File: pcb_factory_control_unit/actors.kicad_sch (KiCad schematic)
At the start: 65 parts, among them J17 STEP1, J18 STEP2, J30 Valve, Q1 IRLML6344, Q2 IRLML6344, Q3 IRLML6344, Q5 IRLML6344, Q6 IRLML6344, U11 74AHCT125, U7 TMC2209, U8 TMC2209

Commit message: Changed LED ReverseMount Footprint, Removed PullUp, HSOS Logo
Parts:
- D2, D3, D4, D5, D8: footprint liebler_OPTO:LED_1206_3216Metric_ReverseMount -> LED_SMD:LED_1206_3216Metric_ReverseMount_Hole1.8x2.4mm

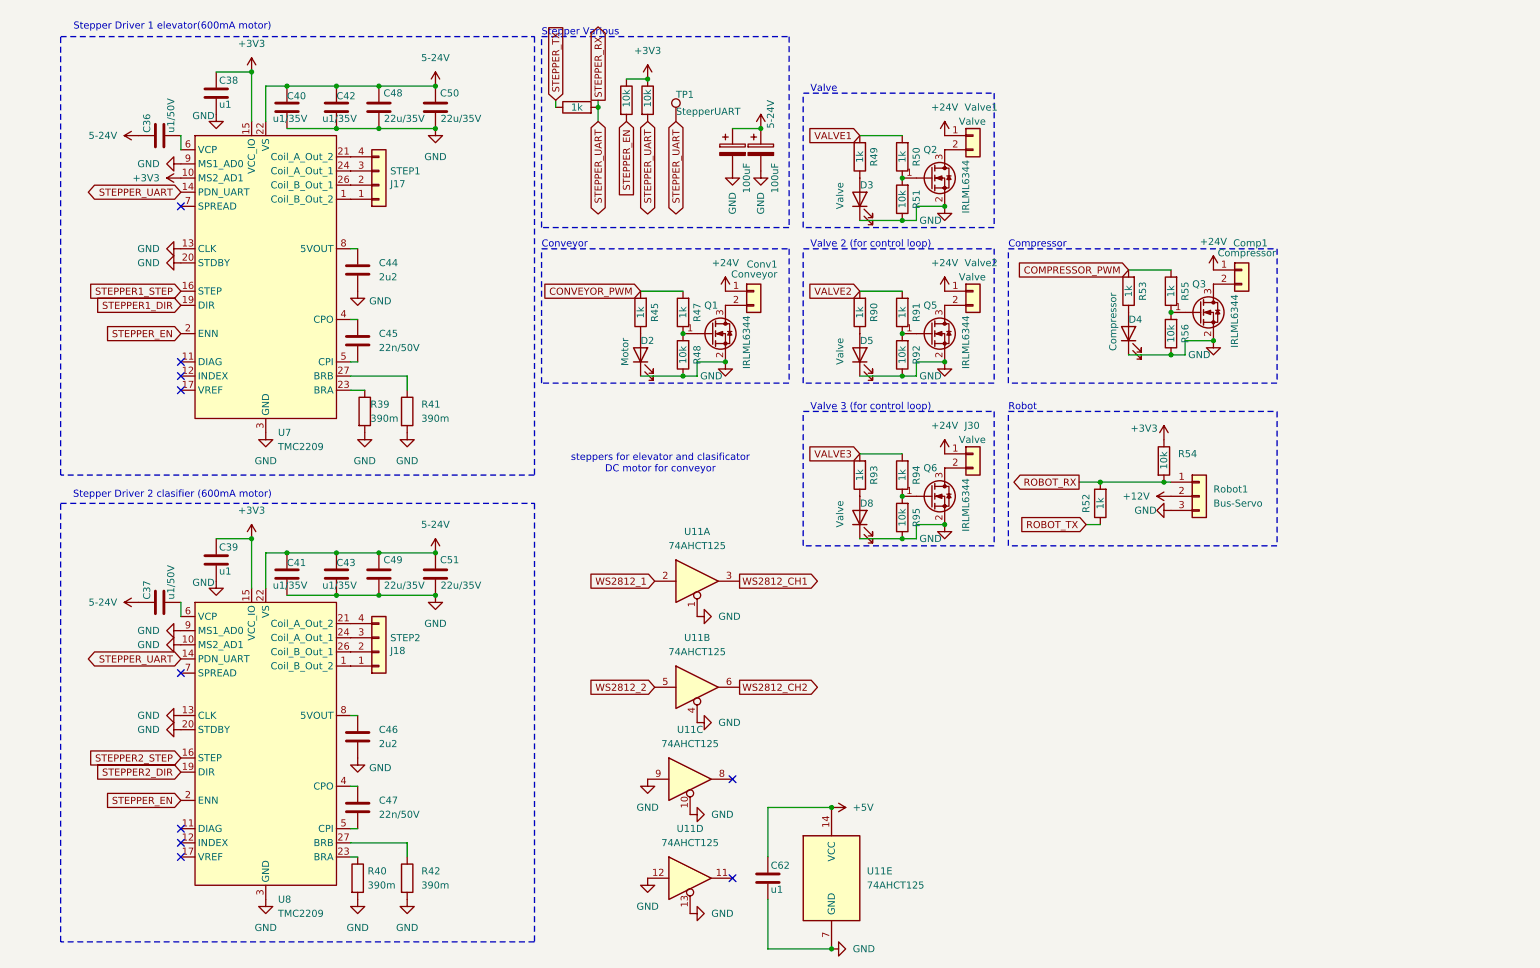
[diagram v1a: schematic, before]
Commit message: Control Unit PCB: schematic rework (PSU, MX26631DL, XL6009 module, ERC fixes), new placement on 90 mm high board
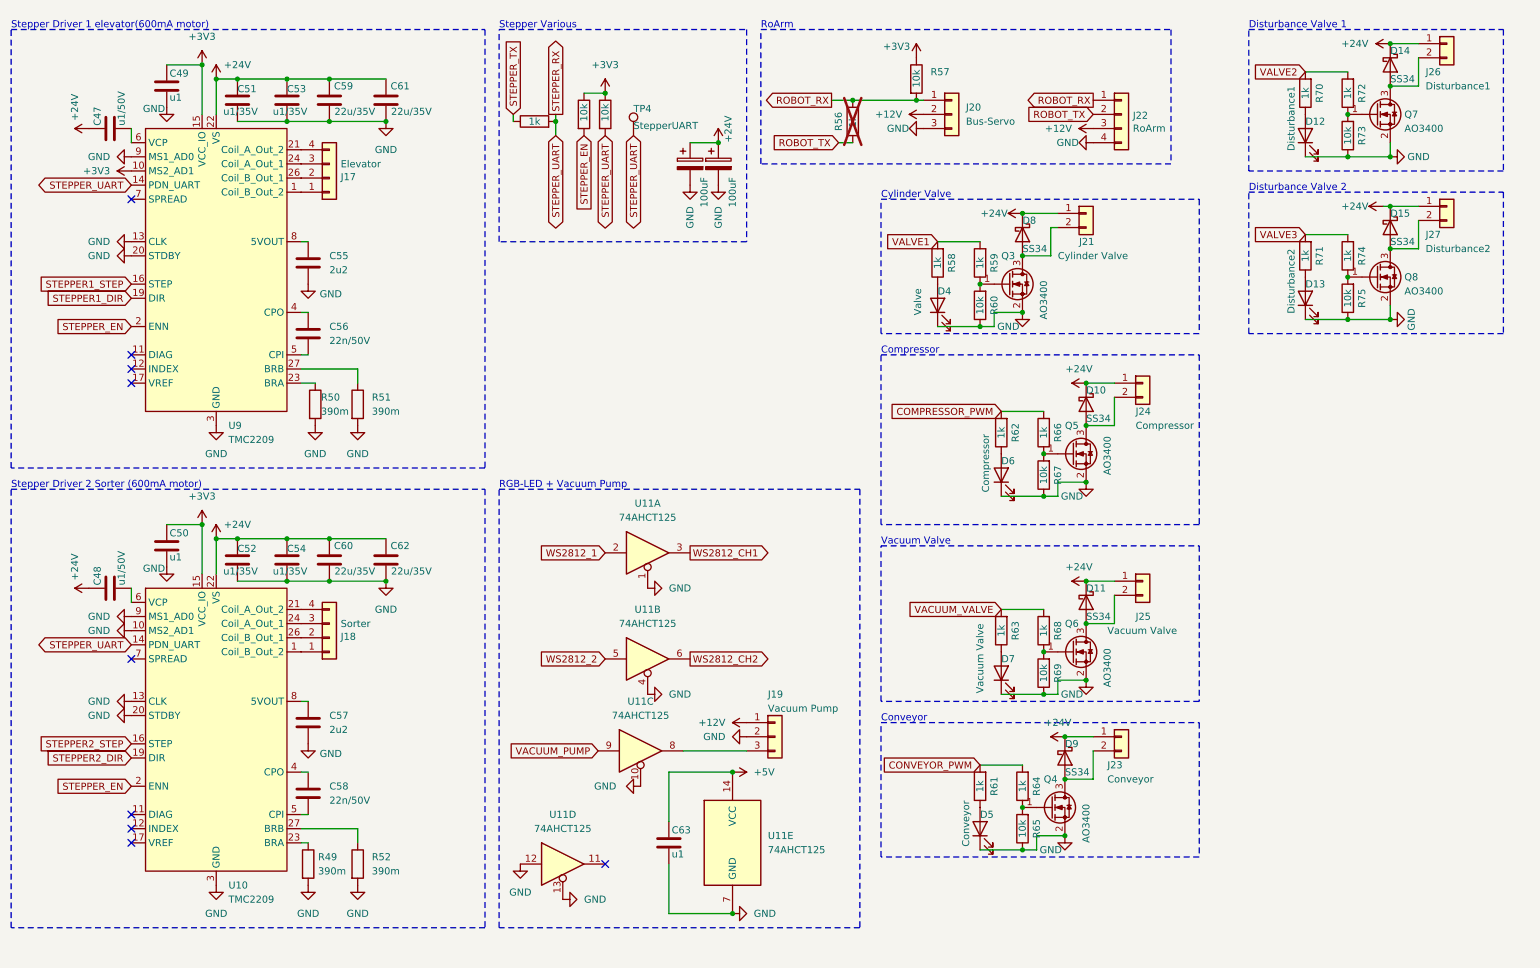
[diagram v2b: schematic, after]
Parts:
- removed J30, Valve1, Valve2: Valve, liebler_CONN:PhoenixContact_MC_1,5_2-G-3.5_1x02_P3.50mm_Horizontal_smallerCourtyard, symbol Connector_Generic:Conn_01x02
- added D10, D11, D14, D15, D8, D9: SS34, Diode_SMD:D_SMA, symbol Diode:SS34
- added D7: Vacuum Valve, LED_SMD:LED_1206_3216Metric_ReverseMount_Hole1.8x2.4mm, symbol Device:LED
- added J19: Vacuum Pump, liebler_CONN:JST_XH_B3B-XH-A_1x03_P2.50mm_Vertical_smaller, symbol Connector_Generic:Conn_01x03
- added J21: Cylinder Valve, Connector_JST:JST_XH_B2B-XH-A_1x02_P2.50mm_Vertical, symbol Connector_Generic:Conn_01x02
- added J22: RoArm, liebler_CONN:JST_XH_B4B-XH-A_1x04_P2.50mm_Vertical_smaller, symbol Connector_Generic:Conn_01x04
- added J25: Vacuum Valve, Connector_JST:JST_XH_B2B-XH-A_1x02_P2.50mm_Vertical, symbol Connector_Generic:Conn_01x02
- added J26: Disturbance1, Connector_JST:JST_XH_B2B-XH-A_1x02_P2.50mm_Vertical, symbol Connector_Generic:Conn_01x02
- added J27: Disturbance2, Connector_JST:JST_XH_B2B-XH-A_1x02_P2.50mm_Vertical, symbol Connector_Generic:Conn_01x02
- added Q6: AO3400, Package_TO_SOT_SMD:SOT-23, symbol Transistor_FET:IRLML0030
- added R63, R68: 1k, Resistor_SMD:R_0402_1005Metric, symbol Device:R
- added R69: 10k, Resistor_SMD:R_0402_1005Metric, symbol Device:R
- D12: renamed from D5; value Valve -> Disturbance1
- D13: renamed from D8; value Valve -> Disturbance2
- D5: renamed from D2; value Motor -> Conveyor
- J17: value STEP1 -> Elevator
- J18: value STEP2 -> Sorter
- Q3: renamed from Q2; value IRLML6344 -> AO3400
- Q4: renamed from Q1; value IRLML6344 -> AO3400
- Q5: renamed from Q3; value IRLML6344 -> AO3400
- Q7: renamed from Q5; value IRLML6344 -> AO3400
- Q8: renamed from Q6; value IRLML6344 -> AO3400
- R56: renamed from R52; footprint Resistor_SMD:R_0402_1005Metric -> Resistor_SMD:R_0805_2012Metric_Pad1.20x1.40mm_HandSolder; now not fitted
- renumbered C36 to C47, C37 to C48, C38 to C49, C39 to C50, C40 to C51, C41 to C52, C42 to C53, C43 to C54, C44 to C55, C45 to C56, C46 to C57, C47 to C58, C48 to C59, C49 to C60, C50 to C61, C51 to C62, C62 to C63, C52 to C64, C53 to C65, D3 to D4, D4 to D6, Robot1 to J20, Conv1 to J23, Comp1 to J24, R40 to R49, R39 to R50, R41 to R51, R42 to R52, R43 to R53, R44 to R54, R46 to R55, R54 to R57, R49 to R58, R50 to R59, R51 to R60, R45 to R61, R53 to R62, R47 to R64, R48 to R65, R55 to R66, R56 to R67, R90 to R70, R93 to R71, R91 to R72, R92 to R73, R94 to R74, R95 to R75, TP1 to TP4, U8 to U10, U7 to U9
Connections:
- net 5-24V is gone; now on net +24V: C47.1, C48.1, C51.1, C52.1, C53.1, C54.1, C59.2, C60.2, C61.2, C62.2, C64.1, C65.1, U10.22 (VS), U10.28 (VS), U9.22 (VS), U9.28 (VS)
- net +12V: now also J19.1 (Pin_1), J22.3 (Pin_3)
- net +24V: now also D10.1 (K), D11.1 (K), D14.1 (K), D15.1 (K), D8.1 (K), D9.1 (K), J21.1 (Pin_1), J25.1 (Pin_1), J26.1 (Pin_1), J27.1 (Pin_1)
- net GND: now also D7.1 (K), J19.2 (Pin_2), J22.4 (Pin_4), Q6.2 (S), R69.1; no longer U11.9
- net ROBOT_RX: now also J22.1 (Pin_1)
- net ROBOT_TX: now also J22.2 (Pin_2)
- net at J23.2 (Pin_2), Q4.3 (D): now also D9.2 (A)
- net at Q8.3 (D): now also D15.2 (A), J27.2 (Pin_2)
- net at J24.2 (Pin_2), Q5.3 (D): now also D10.2 (A)
- net at U11.8: now also J19.3 (Pin_3)
- net at Q7.3 (D): now also D14.2 (A), J26.2 (Pin_2)
- net at Q3.3 (D): now also D8.2 (A), J21.2 (Pin_2)
- new net: D7.2 (A), R63.1
- new net: Q6.1 (G), R68.1, R69.2
- new net: D11.2 (A), J25.2 (Pin_2), Q6.3 (D)
- new net VACUUM_PUMP: U11.9
- new net VACUUM_VALVE: R63.2, R68.2
- no-connect marks 10 -> 9
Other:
- note added: "Cylinder Valve"
- note added: "Disturbance Valve 1"
- note added: "Disturbance Valve 2"
- note added: "RGB-LED + Vacuum Pump"
- note added: "RoArm"
- note added: "Stepper Driver 2 Sorter (600mA motor)"
- note added: "Vacuum Valve"
- note removed: "Robot"
- note removed: "Stepper Driver 2 clasifier (600mA motor)"
- note removed: "Valve"
- note removed: "Valve 2 (for control loop)"
- note removed: "Valve 3 (for control loop)"
- note removed: "steppers for elevator and clasificator DC motor for conveyor"
- moved on the sheet: C47, C48, C49, C50, C51, C52, C53, C54, C55, C56, C57, C58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

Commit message: PCB WIP
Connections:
- net CONVEYOR_PWM: no longer R61.2, R64.2
- new net: R61.2, R64.2
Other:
- moved on the sheet: D11, D4, D5, D7, D8, D9, J21, J23, J25, Q3, Q4, Q6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

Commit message: WIP PCB
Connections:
- net CONVEYOR_PWM: now also R61.2, R64.2
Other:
- moved on the sheet: D12, D13, D14, D15, D4, D8, J21, J26, J27, Q3, Q7, Q8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

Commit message: PCB WIP
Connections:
- net WS2812_1: now also U11.5; no longer U11.2
- net WS2812_2: now also U11.2; no longer U11.5
- net WS2812_CH1: now also U11.6; no longer U11.3
- net WS2812_CH2: now also U11.3; no longer U11.6
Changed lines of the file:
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@@
 	(global_label "WS2812_CH1"
 		(shape output)
-		(at 135.89 109.22 0)
+		(at 135.89 128.27 0)
 		(fields_autoplaced yes)
 		(effects
@@
 		)
 		(property "Intersheetrefs" "${INTERSHEET_REFS}"
-			(at 151.1517 109.22 0)
+			(at 151.1517 128.27 0)
 			(hide yes)
 			(show_name no)
@@
 	(global_label "WS2812_1"
 		(shape input)
-		(at 120.65 109.22 180)
-		(fields_autoplaced yes)
-		(effects
-			(font
-				(size 1.27 1.27)
-			)
-			(justify right)
-		)
-		(property "Intersheetrefs" "${INTERSHEET_REFS}"
-			(at 107.9888 109.22 0)
+		(at 120.65 128.27 180)
+		(fields_autoplaced yes)
+		(effects
+			(font
+				(size 1.27 1.27)
+			)
+			(justify right)
+		)
+		(property "Intersheetrefs" "${INTERSHEET_REFS}"
+			(at 107.9888 128.27 0)
 			(hide yes)
 			(show_name no)
@@
 	(global_label "WS2812_CH2"
 		(shape output)
-		(at 135.89 128.27 0)
+		(at 135.89 109.22 0)
 		(fields_autoplaced yes)
 		(effects
@@
 		)
 		(property "Intersheetrefs" "${INTERSHEET_REFS}"
-			(at 151.1517 128.27 0)
+			(at 151.1517 109.22 0)
 			(hide yes)
 			(show_name no)
@@
 	(global_label "WS2812_2"
 		(shape input)
-		(at 120.65 128.27 180)
-		(fields_autoplaced yes)
-		(effects
-			(font
-				(size 1.27 1.27)
-			)
-			(justify right)
-		)
-		(property "Intersheetrefs" "${INTERSHEET_REFS}"
-			(at 107.9888 128.27 0)
-			(hide yes)
-			(show_name no)
+		(at 120.65 109.22 180)
+		(fields_autoplaced yes)
+		(effects
+			(font
+				(size 1.27 1.27)
+			)
+			(justify right)
+		)
+		(property "Intersheetrefs" "${INTERSHEET_REFS}"
+			(at 107.9888 109.22 0)
+			(hide yes)
+			(show_name no)

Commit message: WIP
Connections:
- net +24V: no longer C47.1, C48.1, C51.1, C52.1, C53.1, C54.1, C59.2, C60.2, C61.2, C62.2, C64.1, C65.1, U10.22 (VS), U10.28 (VS), U9.22 (VS), U9.28 (VS)
- new net +20V: C47.1, C48.1, C51.1, C52.1, C53.1, C54.1, C59.2, C60.2, C61.2, C62.2, C64.1, C65.1, U10.22 (VS), U10.28 (VS), U9.22 (VS), U9.28 (VS)

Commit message: FCB ready for review
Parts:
- removed Q3, Q4, Q5, Q6, Q7, Q8: AO3400, Package_TO_SOT_SMD:SOT-23, symbol Transistor_FET:IRLML0030
- added Q10, Q4, Q5, Q6, Q7, Q8: 40N06D, Package_SON:VSON-8_3.3x3.3mm_P0.65mm_NexFET, symbol Transistor_FET:CSD18543Q3A
- J20: value Bus-Servo -> RoArm
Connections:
- net +24V: now also J23.2 (Pin_2), J24.2 (Pin_2); no longer J23.1 (Pin_1), J24.1 (Pin_1)
- net GND: now also Q10.1 (S), Q10.2 (S), Q10.3 (S), Q4.1 (S), Q4.2 (S), Q4.3 (S), Q5.1 (S), Q5.2 (S), Q5.3 (S), Q6.1 (S), Q6.2 (S), Q6.3 (S), Q7.1 (S), Q7.2 (S), Q7.3 (S), Q8.1 (S), Q8.2 (S), Q8.3 (S)
- net at R72.1, R73.2: now also Q8.4 (G)
- net at D15.2 (A), J27.2 (Pin_2): now also Q7.5 (D)
- net at D8.2 (A), J21.2 (Pin_2): now also Q10.5 (D)
- net at R74.1, R75.2: now also Q7.4 (G)
- net at R64.1, R65.2: now also Q5.4 (G)
- net at D9.2 (A): now also J23.1 (Pin_1), Q5.5 (D); no longer J23.2 (Pin_2)
- net at R66.1, R67.2: now also Q4.4 (G)
- net at D10.2 (A): now also J24.1 (Pin_1), Q4.5 (D); no longer J24.2 (Pin_2)
- net at R68.1, R69.2: now also Q6.4 (G)
- net at D14.2 (A), J26.2 (Pin_2): now also Q8.5 (D)
- net at D11.2 (A), J25.2 (Pin_2): now also Q6.5 (D)
- net at R59.1, R60.2: now also Q10.4 (G)
